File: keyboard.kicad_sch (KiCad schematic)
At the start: 26 parts, among them IC2 80C51, IC3 74LS145, IC4 74LS145, IC7 74LS366, IC9 74LS241

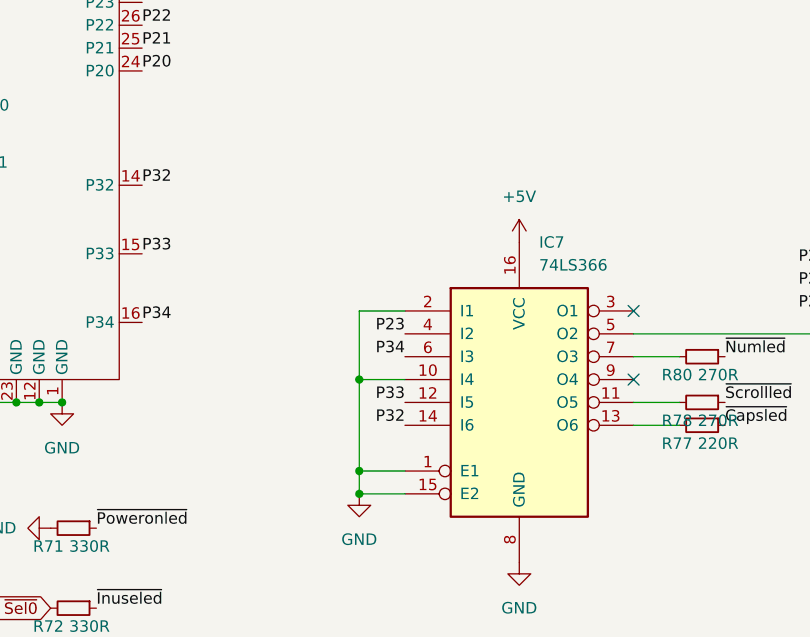
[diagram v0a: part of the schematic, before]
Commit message: add cheeky mean well power swap
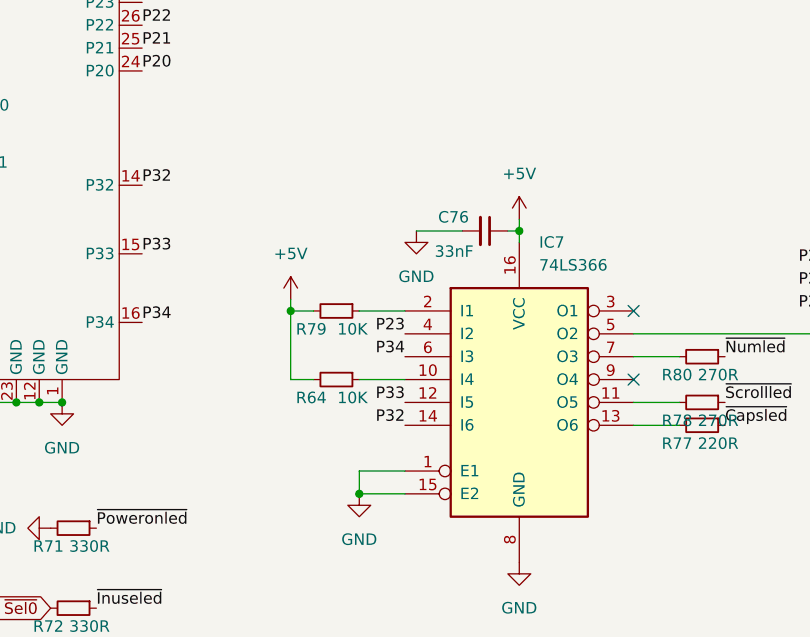
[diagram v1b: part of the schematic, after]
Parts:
- added C76: 33nF, Capacitor_SMD:C_0805_2012Metric, symbol Device:C_Small
- added R64, R79: 10K, Resistor_SMD:R_0805_2012Metric, symbol Device:R_Small
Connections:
- net +5V: now also C76.1, R64.2, R79.2
- net GND: now also C76.2; no longer IC7.10 (I4), IC7.2 (I1)
- new net: IC7.10 (I4), R64.1
- new net: IC7.2 (I1), R79.1

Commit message: implement video routing
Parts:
- FS5: footprint Fuse:Fuse_1206_3216Metric -> Fuse:Fuse_2512_6332Metric
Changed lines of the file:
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@@
 			)
 		)
-		(property "Footprint" "Fuse:Fuse_1206_3216Metric"
+		(property "Footprint" "Fuse:Fuse_2512_6332Metric"
 			(at 39.37 68.58 0)
 			(effects

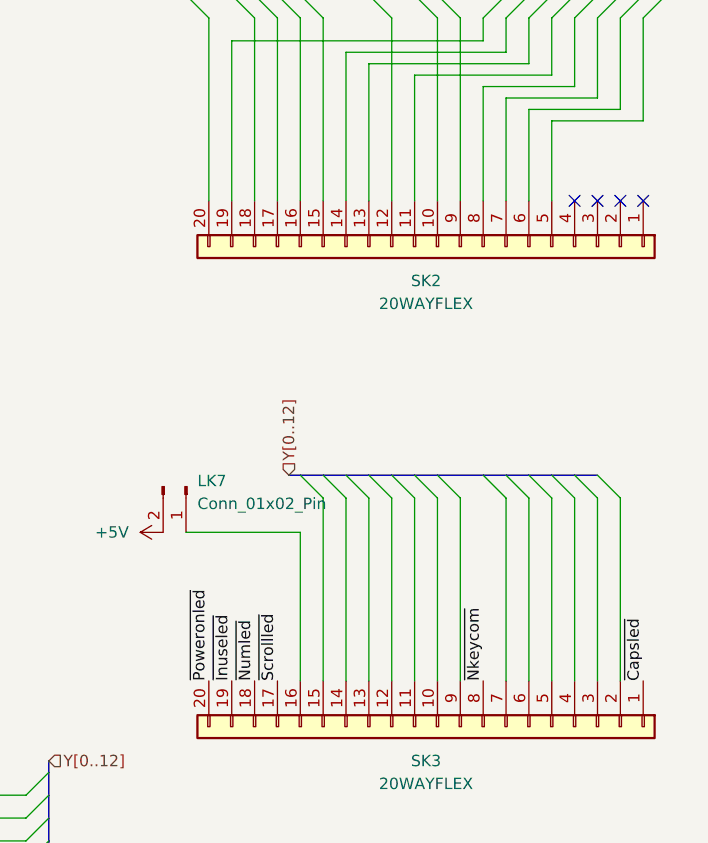
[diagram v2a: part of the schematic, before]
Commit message: video and keyboard routing
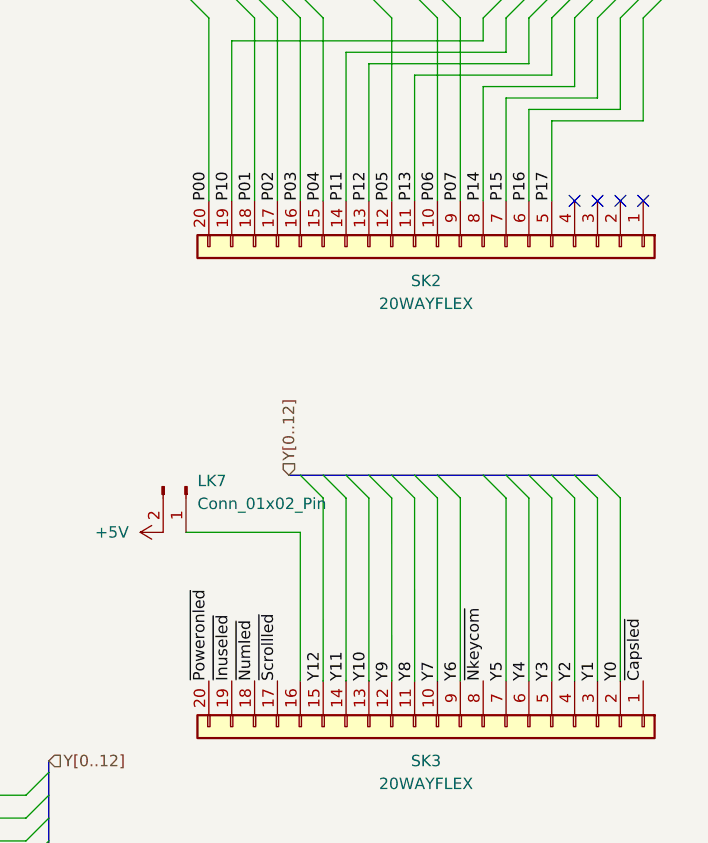
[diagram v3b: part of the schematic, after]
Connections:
- net P00: now also SK2.20 (Pin_20)
- net P01: now also SK2.18 (Pin_18)
- net P02: now also SK2.17 (Pin_17)
- net P03: now also SK2.16 (Pin_16)
- net P04: now also SK2.15 (Pin_15)
- net P05: now also SK2.12 (Pin_12)
- net P06: now also SK2.10 (Pin_10)
- net P07: now also SK2.9 (Pin_9)
- net P10: now also SK2.19 (Pin_19)
- net P11: now also SK2.14 (Pin_14)
- net P12: now also SK2.13 (Pin_13)
- net P13: now also SK2.11 (Pin_11)
- net P14: now also SK2.8 (Pin_8)
- net P15: now also SK2.7 (Pin_7)
- net P16: now also SK2.6 (Pin_6)
- net P17: now also SK2.5 (Pin_5)
- net Y0: now also SK3.2 (Pin_2)
- net Y1: now also SK3.3 (Pin_3)
- net Y10: now also SK3.13 (Pin_13)
- net Y11: now also SK3.14 (Pin_14)
- net Y12: now also SK3.15 (Pin_15)
- net Y2: now also SK3.4 (Pin_4)
- net Y3: now also SK3.5 (Pin_5)
- net Y4: now also SK3.6 (Pin_6)
- net Y5: now also SK3.7 (Pin_7)
- net Y6: now also SK3.9 (Pin_9)
- net Y7: now also SK3.10 (Pin_10)
- net Y8: now also SK3.11 (Pin_11)
- net Y9: now also SK3.12 (Pin_12)

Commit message: keyboard and joystick routing
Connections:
- net P10 is gone; now on net Id0: IC2.2 (P10), LK10.1 (Pin_1), LK12.1 (Pin_1), LK4.1 (Pin_1), LK5.1 (Pin_1), LK8.1 (Pin_1), LK9.1 (Pin_1), SK2.19 (Pin_19)
- net Id0: now also LK12.2 (Pin_2)
- net Id1: now also LK8.2 (Pin_2)
- net Id2: now also LK5.2 (Pin_2)
- net Id3: now also LK4.2 (Pin_2)
- net Id4: now also LK10.2 (Pin_2)
- net Id5: now also LK9.2 (Pin_2)
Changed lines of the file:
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@@
 	)
 	(junction
+		(at 179.07 104.14)
+		(diameter 0)
+		(color 0 0 0 0)
+	)
+	(junction
 		(at 76.2 139.7)
 		(diameter 0)
@@
 	)
 	(junction
+		(at 179.07 101.6)
+		(diameter 0)
+		(color 0 0 0 0)
+	)
+	(junction
 		(at 96.52 177.8)
 		(diameter 0)
@@
 	(wire
 		(pts
+			(xy 179.07 101.6) (xy 179.07 104.14)
+		)
+		(stroke
+			(width 0)
+			(type default)
+		)
+	)
+	(wire
+		(pts
 			(xy 90.17 182.88) (xy 104.14 182.88)
 		)
@@
 		)
 	)
+	(label "Id2"
+		(at 163.83 107.95 90)
+		(fields_autoplaced yes)
+		(effects
+			(font
+				(size 1.27 1.27)
+			)
+			(justify left bottom)
+		)
+	)
 	(label "Sw2"
 		(at 114.3 102.87 0)
@@
 		)
 	)
+	(label "Id5"
+		(at 140.97 107.95 90)
+		(fields_autoplaced yes)
+		(effects
+			(font
+				(size 1.27 1.27)
+			)
+			(justify left bottom)
+		)
+	)
 	(label "P14"
 		(at 90.17 156.21 0)
@@
 		)
 	)
+	(label "Id1"
+		(at 171.45 107.95 90)
+		(fields_autoplaced yes)
+		(effects
+			(font
+				(size 1.27 1.27)
+			)
+			(justify left bottom)
+		)
+	)
+	(label "Id4"
+		(at 148.59 107.95 90)
+		(fields_autoplaced yes)
+		(effects
+			(font
+				(size 1.27 1.27)
+			)
+			(justify left bottom)
+		)
+	)
 	(label "Yr"
 		(at 64.77 153.67 180)
@@
 		)
 	)
+	(label "Id0"
+		(at 179.07 107.95 90)
+		(fields_autoplaced yes)
+		(effects
+			(font
+				(size 1.27 1.27)
+			)
+			(justify left bottom)
+		)
+	)
 	(label "~{Numled}"
 		(at 226.06 171.45 90)
@@
 		(fields_autoplaced yes)
 		(effects
+			(font
+				(size 1.27 1.27)
+			)
+			(justify left bottom)
+		)
+	)
+	(label "Id3"
+		(at 156.21 107.95 90)
+		(fields_autoplaced yes)
+		(effects

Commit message: more traces
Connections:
- net GND: now also IC9.1 (OEa)
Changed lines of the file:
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@@
+	)
+	(symbol
+		(lib_id "power:GND")
+		(at 88.9 110.49 270)
+		(unit 1)
+		(exclude_from_sim no)
+		(in_bom yes)
+		(on_board yes)
+		(dnp no)
+		(fields_autoplaced yes)
+		(property "Reference" "#PWR0210"
+			(at 82.55 110.49 0)
+			(effects
+				(font
+					(size 1.27 1.27)
+				)
+				(hide yes)
+			)
+		)
+		(property "Value" "GND"
+			(at 85.09 110.4899 90)
+			(effects
+				(font
+					(size 1.27 1.27)
+				)
+				(justify right)
+			)
+		)
+		(property "Footprint" ""
+			(at 88.9 110.49 0)
+			(effects
+				(font
+					(size 1.27 1.27)
+				)
+				(hide yes)
+			)
+		)
+		(property "Datasheet" ""
+			(at 88.9 110.49 0)
+			(effects
+				(font
+					(size 1.27 1.27)
+				)
+				(hide yes)
+			)
+		)
+		(property "Description" "Power symbol creates a global label with name \"GND\" , ground"
+			(at 88.9 110.49 0)
+			(effects
+				(font
+					(size 1.27 1.27)
+				)
+				(hide yes)
+			)
+		)
+		(pin "1"
+		)
+		(instances
+			(project "Acorn-A3010"
+				(path "/999882f3-94f8-4a89-9093-27a47d0cb289/20613dd3-c886-4190-96bd-e62e2e571bea"
+					(reference "#PWR0210")
+					(unit 1)
+				)
+			)
+		)
 	)
 	(symbol

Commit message: yet more traces
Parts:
- added RX2: 4k7, Resistor_THT:R_Axial_DIN0204_L3.6mm_D1.6mm_P5.08mm_Horizontal, symbol Device:R_Small
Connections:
- net +5V: now also RX2.1
- net at IC3.12 (P3), IC7.5 (O2): now also RX2.2
- net Kin renamed Kbkin
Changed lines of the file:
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@@
 	)
 	(junction
+		(at 151.13 243.84)
+		(diameter 0)
+		(color 0 0 0 0)
+	)
+	(junction
 		(at 115.57 170.18)
 		(diameter 0)
@@
 	(wire
 		(pts
-			(xy 144.78 243.84) (xy 166.37 243.84)
+			(xy 144.78 243.84) (xy 151.13 243.84)
 		)
 		(stroke
@@
 	(wire
 		(pts
+			(xy 151.13 240.03) (xy 151.13 243.84)
+		)
+		(stroke
+			(width 0)
+			(type default)
+		)
+	)
+	(wire
+		(pts
 			(xy 156.21 92.71) (xy 163.83 92.71)
 		)
@@
 		)
 	)
+	(wire
+		(pts
+			(xy 151.13 243.84) (xy 166.37 243.84)
+		)
+		(stroke
+			(width 0)
+			(type default)
+		)
+	)
 	(bus
 		(pts
@@
 		)
 	)
-	(global_label "~{Sel0}"
+	(global_label "Kbkin"
 		(shape input)
-		(at 80.01 274.32 180)
+		(at 64.77 224.79 180)
 		(fields_autoplaced yes)
 		(effects
@@
 		)
 		(property "Intersheetrefs" "${INTERSHEET_REFS}"
-			(at 72.852 274.32 0)
+			(at 56.5839 224.79 0)
 			(effects
 				(font
@@
 		)
 	)
-	(global_label "Kin"
-		(shape output)
-		(at 64.77 224.79 180)
+	(global_label "~{Sel0}"
+		(shape input)
+		(at 80.01 274.32 180)
 		(fields_autoplaced yes)
 		(effects
@@
 		)
 		(property "Intersheetrefs" "${INTERSHEET_REFS}"
-			(at 58.761 224.79 0)
+			(at 72.852 274.32 0)
 			(effects
 				(font
@@
 	)
 	(symbol
+		(lib_id "power:+5V")
+		(at 151.13 234.95 0)
+		(unit 1)
+		(exclude_from_sim no)
+		(in_bom yes)
+		(on_board yes)
+		(dnp no)
+		(fields_autoplaced yes)
+		(property "Reference" "#PWR0297"
+			(at 151.13 238.76 0)
+			(effects
+				(font
+					(size 1.27 1.27)
+				)
+				(hide yes)
+			)
+		)
+		(property "Value" "+5V"
+			(at 151.13 229.87 0)
+			(effects
+				(font
+					(size 1.27 1.27)
+				)
+			)
+		)
+		(property "Footprint" ""
+			(at 151.13 234.95 0)
+			(effects
+				(font
+					(size 1.27 1.27)
+				)
+				(hide yes)
+			)
+		)
+		(property "Datasheet" ""
+			(at 151.13 234.95 0)
+			(effects
+				(font
+					(size 1.27 1.27)
+				)
+				(hide yes)
+			)
+		)
+		(property "Description" "Power symbol creates a global label with name \"+5V\""
+			(at 151.13 234.95 0)
+			(effects
+				(font
+					(size 1.27 1.27)
+				)
+				(hide yes)
+			)
+		)
+		(pin "1"
+		)
+		(instances
+			(project "Acorn-A3010"
+				(path "/999882f3-94f8-4a89-9093-27a47d0cb289/20613dd3-c886-4190-96bd-e62e2e571bea"
+					(reference "#PWR0297")
+					(unit 1)
+				)
+			)
+		)
+	)
+	(symbol
 		(lib_id "Acorn:R_Network15_Split")
 		(at 189.23 312.42 0)
@@
 					(unit 1)
 				)
+			)
+		)
+	)
+	(symbol
+		(lib_id "Device:R_Small")
+		(at 151.13 237.49 0)
+		(unit 1)
+		(exclude_from_sim no)
+		(in_bom yes)
+		(on_board yes)
+		(dnp no)
+		(fields_autoplaced yes)
+		(property "Reference" "RX2"
+			(at 153.67 236.2199 0)
+			(effects
+				(font
+					(size 1.27 1.27)
+				)
+				(justify left)
+			)
+		)
+		(property "Value" "4k7"
+			(at 153.67 238.7599 0)
+			(effects
+				(font
+					(size 1.27 1.27)
+				)
+				(justify left)
+			)
+		)
+		(property "Footprint" "Resistor_THT:R_Axial_DIN0204_L3.6mm_D1.6mm_P5.08mm_Horizontal"
+			(at 151.13 237.49 0)
+			(effects
+				(font
+					(size 1.27 1.27)
+				)
+				(hide yes)
+			)
+		)
+		(property "Datasheet" "~"
+			(at 151.13 237.49 0)
+			(effects
+				(font
+					(size 1.27 1.27)
+				)
+				(hide yes)
+			)
+		)
+		(property "Description" "Resistor, small symbol"
+			(at 151.13 237.49 0)
+			(effects
+				(font
+					(size 1.27 1.27)
+				)
+				(hide yes)
+			)
+		)
+		(pin "1"
+		)
+		(pin "2"
+		)
+		(instances
+			(project ""
+				(path "/999882f3-94f8-4a89-9093-27a47d0cb289/20613dd3-c886-4190-96bd-e62e2e571bea"
+					(reference "RX2")
+					(unit 1)
+				)

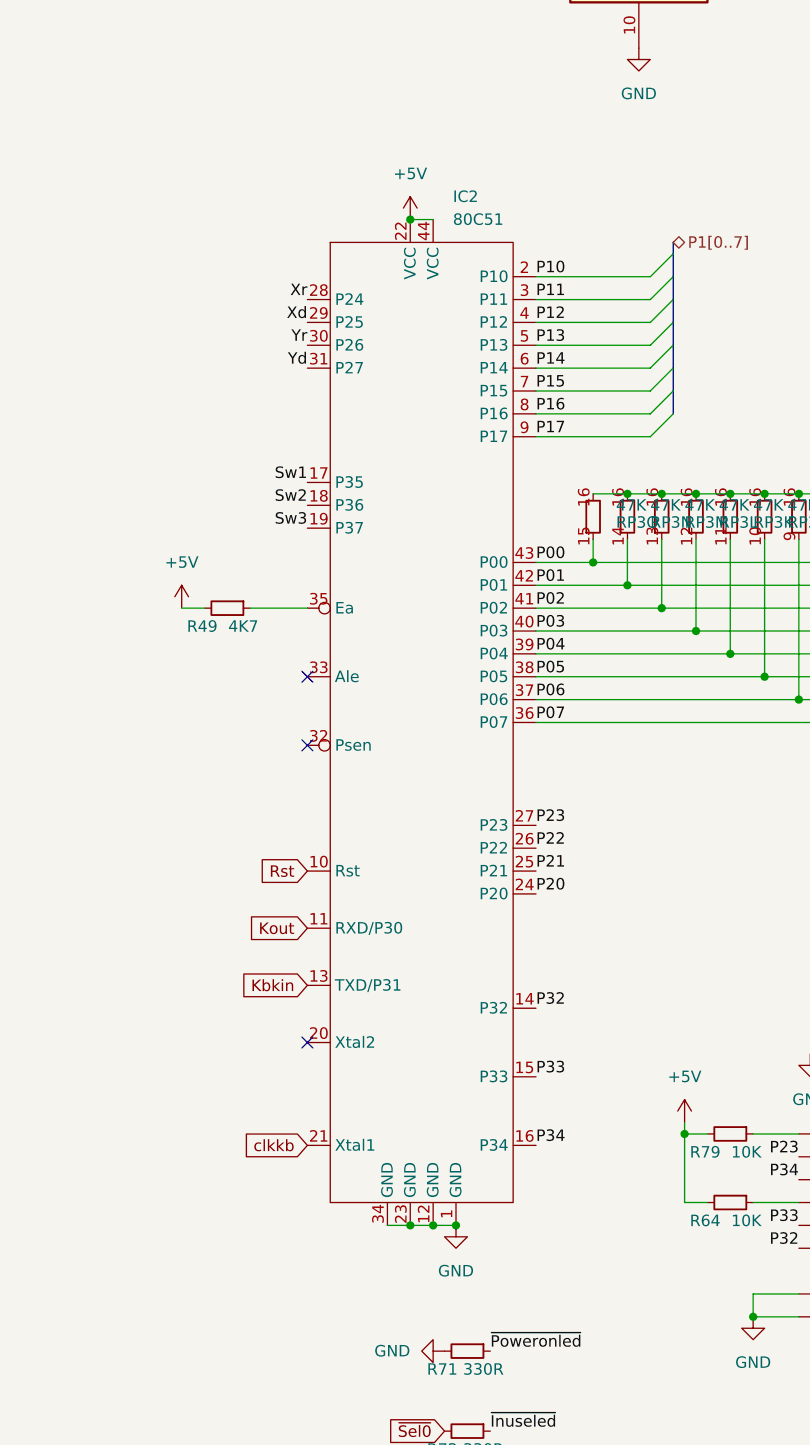
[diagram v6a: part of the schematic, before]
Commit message: progress power and keyboard
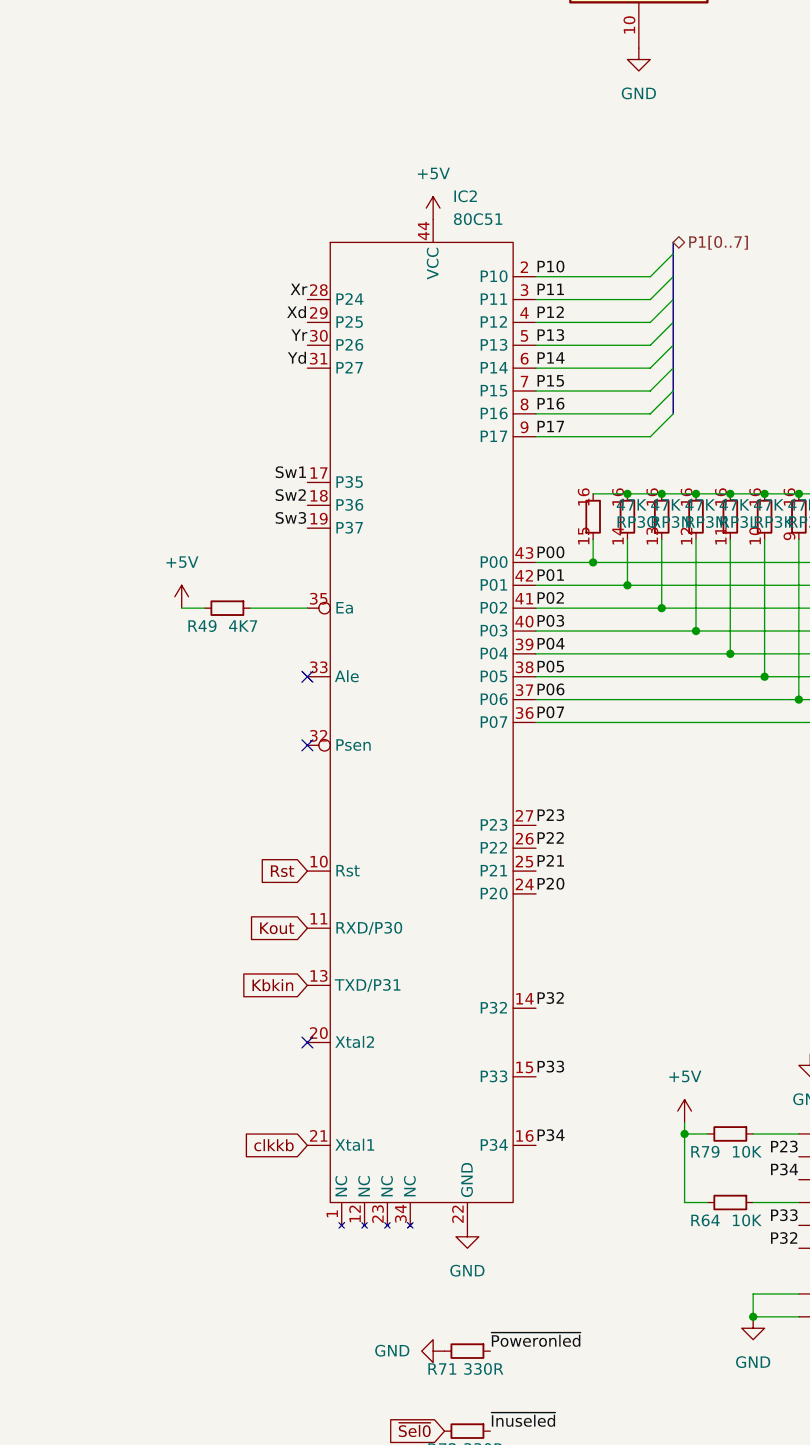
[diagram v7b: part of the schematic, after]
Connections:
- net +5V: no longer IC2.22 (VCC)
- net GND: now also IC2.22 (GND); no longer IC2.1 (GND), IC2.12 (GND), IC2.23 (GND), IC2.34 (GND)
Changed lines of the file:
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@@
 	)
 	(junction
-		(at 76.2 139.7)
-		(diameter 0)
-		(color 0 0 0 0)
-	)
-	(junction
 		(at 71.12 66.04)
 		(diameter 0)
@@
 	)
 	(junction
-		(at 81.28 251.46)
-		(diameter 0)
-		(color 0 0 0 0)
-	)
-	(junction
-		(at 76.2 251.46)
-		(diameter 0)
-		(color 0 0 0 0)
-	)
-	(junction
 		(at 151.13 243.84)
 		(diameter 0)
@@
 	)
 	(junction
-		(at 78.74 251.46)
-		(diameter 0)
-		(color 0 0 0 0)
-	)
-	(junction
 		(at 171.45 92.71)
 		(diameter 0)
@@
 	(wire
 		(pts
-			(xy 76.2 139.7) (xy 78.74 139.7)
-		)
-		(stroke
-			(width 0)
-			(type default)
-		)
-	)
-	(wire
-		(pts
 			(xy 100.33 175.26) (xy 100.33 180.34)
 		)
@@
 	(wire
 		(pts
-			(xy 78.74 251.46) (xy 81.28 251.46)
-		)
-		(stroke
-			(width 0)
-			(type default)
-		)
-	)
-	(wire
-		(pts
 			(xy 90.17 163.83) (xy 102.87 163.83)
 		)
@@
 	(wire
 		(pts
-			(xy 73.66 251.46) (xy 76.2 251.46)
-		)
-		(stroke
-			(width 0)
-			(type default)
-		)
-	)
-	(wire
-		(pts
 			(xy 179.07 91.44) (xy 179.07 92.71)
 		)
@@
 		)
 	)
-	(wire
-		(pts
-			(xy 76.2 251.46) (xy 78.74 251.46)
-		)
-		(stroke
-			(width 0)
-			(type default)
-		)
-	)
 	(bus
 		(pts
@@
 	(symbol
 		(lib_id "power:+5V")
-		(at 76.2 139.7 0)
+		(at 78.74 139.7 0)
 		(unit 1)
 		(exclude_from_sim no)
@@
 		(fields_autoplaced yes)
 		(property "Reference" "#PWR0163"
-			(at 76.2 143.51 0)
+			(at 78.74 143.51 0)
 			(effects
 				(font
@@
 		)
 		(property "Value" "+5V"
-			(at 76.2 134.62 0)
+			(at 78.74 134.62 0)
 			(effects
 				(font
@@
 		)
 		(property "Footprint" ""
-			(at 76.2 139.7 0)
+			(at 78.74 139.7 0)
 			(effects
 				(font
@@
 		)
 		(property "Datasheet" ""
-			(at 76.2 139.7 0)
+			(at 78.74 139.7 0)
 			(effects
 				(font
@@
 		)
 		(property "Description" "Power symbol creates a global label with name \"+5V\""
-			(at 76.2 139.7 0)
+			(at 78.74 139.7 0)
 			(effects
 				(font
@@
 	)
 	(symbol
-		(lib_id "power:GND")
-		(at 81.28 251.46 0)
+		(lib_id "Device:R_Small")
+		(at 151.13 237.49 0)
 		(unit 1)
 		(exclude_from_sim no)
@@
 		(dnp no)
 		(fields_autoplaced yes)
-		(property "Reference" "#PWR0161"
-			(at 81.28 257.81 0)
+		(property "Reference" "RX2"
+			(at 153.67 236.2199 0)
 			(effects
 				(font
 					(size 1.27 1.27)
 				)
-				(hide yes)
+				(justify left)
 			)
 		)
-		(property "Value" "GND"
-			(at 81.28 256.54 0)
+		(property "Value" "4k7"
+			(at 153.67 238.7599 0)
 			(effects
 				(font
 					(size 1.27 1.27)
 				)
+				(justify left)
 			)
 		)
-		(property "Footprint" ""
-			(at 81.28 251.46 0)
+		(property "Footprint" "Resistor_THT:R_Axial_DIN0204_L3.6mm_D1.6mm_P5.08mm_Horizontal"
+			(at 151.13 237.49 0)
 			(effects
 				(font
@@
 			)
 		)
-		(property "Datasheet" ""
-			(at 81.28 251.46 0)
+		(property "Datasheet" "~"
+			(at 151.13 237.49 0)
 			(effects
 				(font
@@
 			)
 		)
-		(property "Description" "Power symbol creates a global label with name \"GND\" , ground"
-			(at 81.28 251.46 0)
+		(property "Description" "Resistor, small symbol"
+			(at 151.13 237.49 0)
 			(effects
 				(font
@@
 		(pin "1"
 		)
+		(pin "2"
+		)
 		(instances
-			(project "Acorn-A3010"
+			(project ""
 				(path "/999882f3-94f8-4a89-9093-27a47d0cb289/20613dd3-c886-4190-96bd-e62e2e571bea"
-					(reference "#PWR0161")
+					(reference "RX2")
 					(unit 1)
 				)
@@
 	)
 	(symbol
-		(lib_id "Device:R_Small")
-		(at 151.13 237.49 0)
+		(lib_id "power:GND")
+		(at 82.55 251.46 0)
 		(unit 1)
 		(exclude_from_sim no)
@@
 		(dnp no)
 		(fields_autoplaced yes)
-		(property "Reference" "RX2"
-			(at 153.67 236.2199 0)
+		(property "Reference" "#PWR0161"
+			(at 82.55 257.81 0)
 			(effects
 				(font
 					(size 1.27 1.27)
 				)
-				(justify left)
+				(hide yes)
 			)
 		)
-		(property "Value" "4k7"
-			(at 153.67 238.7599 0)
+		(property "Value" "GND"
+			(at 82.55 256.54 0)
 			(effects
 				(font
 					(size 1.27 1.27)
 				)
-				(justify left)
 			)
 		)
-		(property "Footprint" "Resistor_THT:R_Axial_DIN0204_L3.6mm_D1.6mm_P5.08mm_Horizontal"
-			(at 151.13 237.49 0)
+		(property "Footprint" ""
+			(at 82.55 251.46 0)
 			(effects
 				(font
@@
 			)
 		)
-		(property "Datasheet" "~"
-			(at 151.13 237.49 0)
+		(property "Datasheet" ""
+			(at 82.55 251.46 0)
 			(effects
 				(font
@@
 			)
 		)
-		(property "Description" "Resistor, small symbol"
-			(at 151.13 237.49 0)
+		(property "Description" "Power symbol creates a global label with name \"GND\" , ground"
+			(at 82.55 251.46 0)
 			(effects
 				(font
@@
 		(pin "1"
 		)
-		(pin "2"
-		)
 		(instances
-			(project ""
+			(project "Acorn-A3010"
 				(path "/999882f3-94f8-4a89-9093-27a47d0cb289/20613dd3-c886-4190-96bd-e62e2e571bea"
-					(reference "RX2")
+					(reference "#PWR0161")
 					(unit 1)
 				)
